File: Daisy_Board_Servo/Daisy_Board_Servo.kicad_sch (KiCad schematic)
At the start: 58 parts, among them IC1 PCA9685PW, IC2 TJA1050T_CM, IC3 LSM6DS3TR-C, J1 SM04B-SRSS-TB, J10 Conn_01x03_Pin, J11 Conn_01x03_Pin, J12 Conn_01x03_Pin, J13 Conn_01x03_Pin, J14 Conn_01x03_Pin, J15 Conn_01x03_Pin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

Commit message: Done Servo
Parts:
- added C2, C3: 100nF 50V, Capacitor_SMD:C_0402_1005Metric, symbol Device:C
- added D3: SS34, Diode_SMD:D_SOD-123, symbol Diode:1N5820
- added D4: ESD9XD, Diode_SMD:D_SOD-523, symbol Device:D
- added D5: ESD9X, Diode_SMD:D_SOD-523, symbol Device:D
- added IC4: ACS712ELCTR-05B-T, SOIC127P600X175-8N, symbol SamacSys_Parts:ACS712ELCTR-05B-T
- added JP3: SolderJumper_3_Bridged12, Jumper:SolderJumper-3_P1.3mm_Bridged2Bar12_RoundedPad1.0x1.5mm, symbol Jumper:SolderJumper_3_Bridged12
- added JP5: SolderJumper_2_Open, Jumper:SolderJumper-2_P1.3mm_Open_RoundedPad1.0x1.5mm, symbol Jumper:SolderJumper_2_Open
- added R24: 22k, Resistor_SMD:R_0402_1005Metric, symbol Device:R
- added R25: 2.2k, Resistor_SMD:R_0402_1005Metric, symbol Device:R
- added VR2: ~, Library:EY9 reg board, symbol Personal:Reg_Board
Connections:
- net +24V: now also D3.2 (A), JP3.3 (B)
- net +3.3V: now also D4.1 (K)
- net +5V: now also IC4.8 (VCC), JP5.2 (B)
- net GND: now also C2.2, C3.2, D5.2 (A), IC4.3 (IP-_1), IC4.4 (IP-_2), IC4.5 (GND), R24.2, VR2.1 (Out-), VR2.4 (In-); no longer J10.1 (Pin_1), J11.1 (Pin_1), J12.1 (Pin_1), J13.1 (Pin_1), J14.1 (Pin_1), J15.1 (Pin_1), J3.1 (Pin_1), J9.1 (Pin_1)
- net ServoPower: now also JP3.2 (C)
- net Current Sense: now reaches U1.1 (A5_GPIO5_MISO)
- net Current Sense: now also C3.1, D4.2 (A), D5.1 (K), R24.1, R25.1
- new net: C2.1, IC4.6 (FILTER)
- new net: JP3.1 (A), JP5.1 (A), VR2.2 (Out+)
- new net: IC4.7 (VIOUT), R25.2
- new net: D3.1 (K), VR2.3 (In+)
- new net ServoGND: IC4.1 (IP+_1), IC4.2 (IP+_2), J10.1 (Pin_1), J11.1 (Pin_1), J12.1 (Pin_1), J13.1 (Pin_1), J14.1 (Pin_1), J15.1 (Pin_1), J3.1 (Pin_1), J9.1 (Pin_1)
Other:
- moved on the sheet: C1, J10, J11, J12, J13, J14, J15, J3, J9, R18, R19, R20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

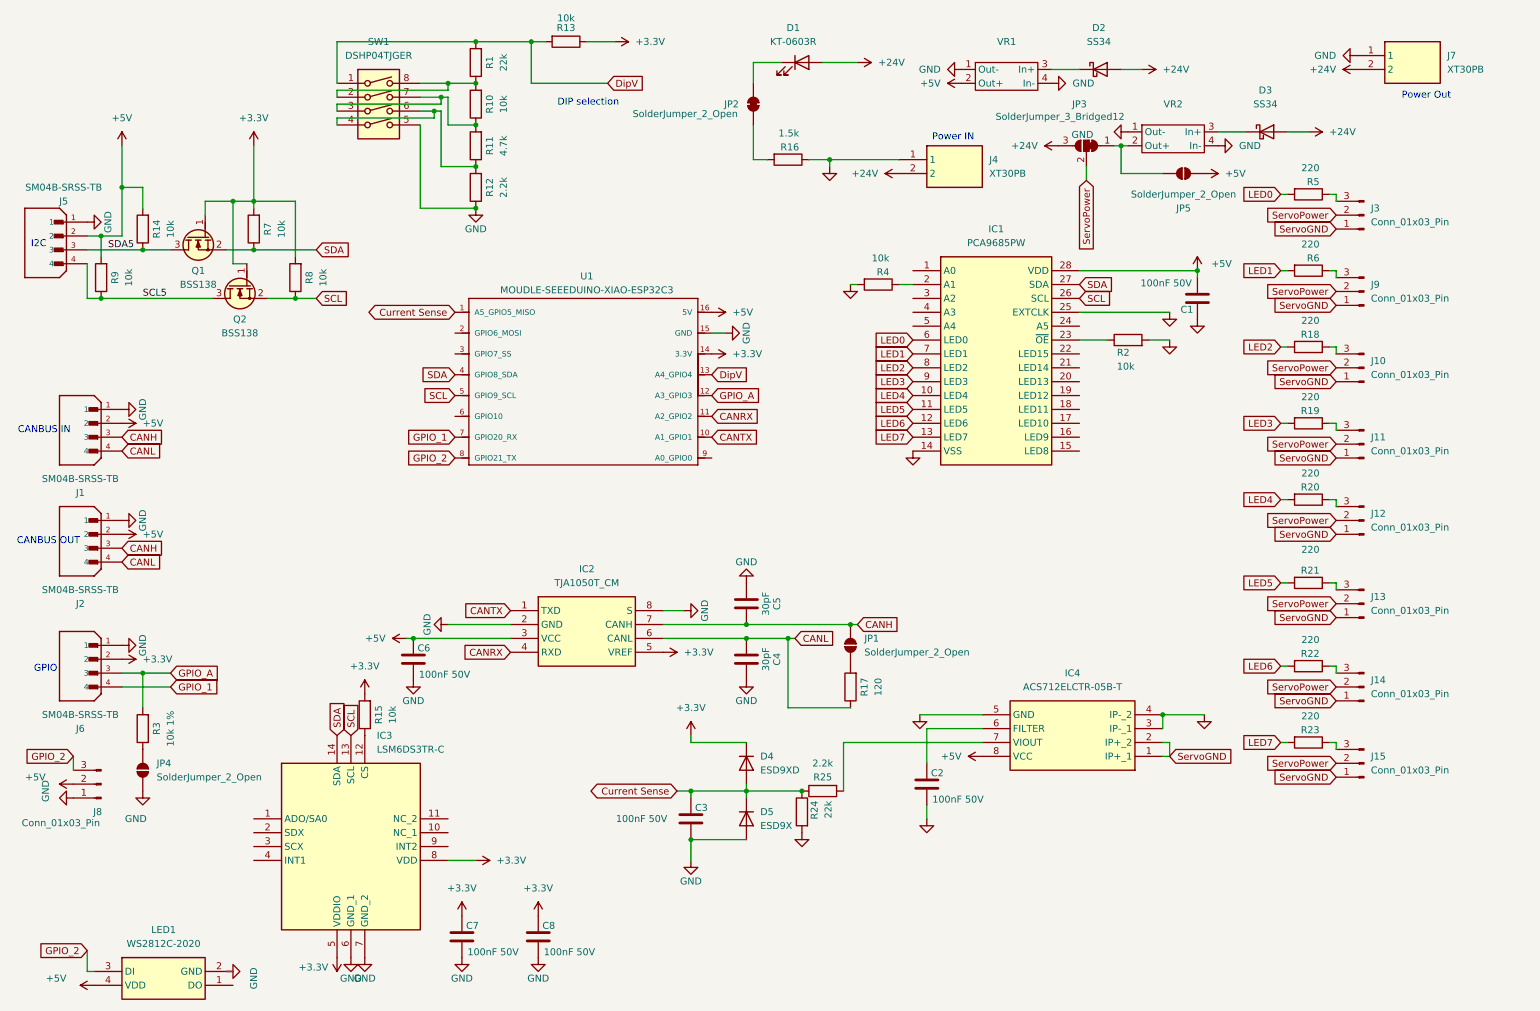
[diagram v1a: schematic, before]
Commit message: panel updates for lower QTY parts
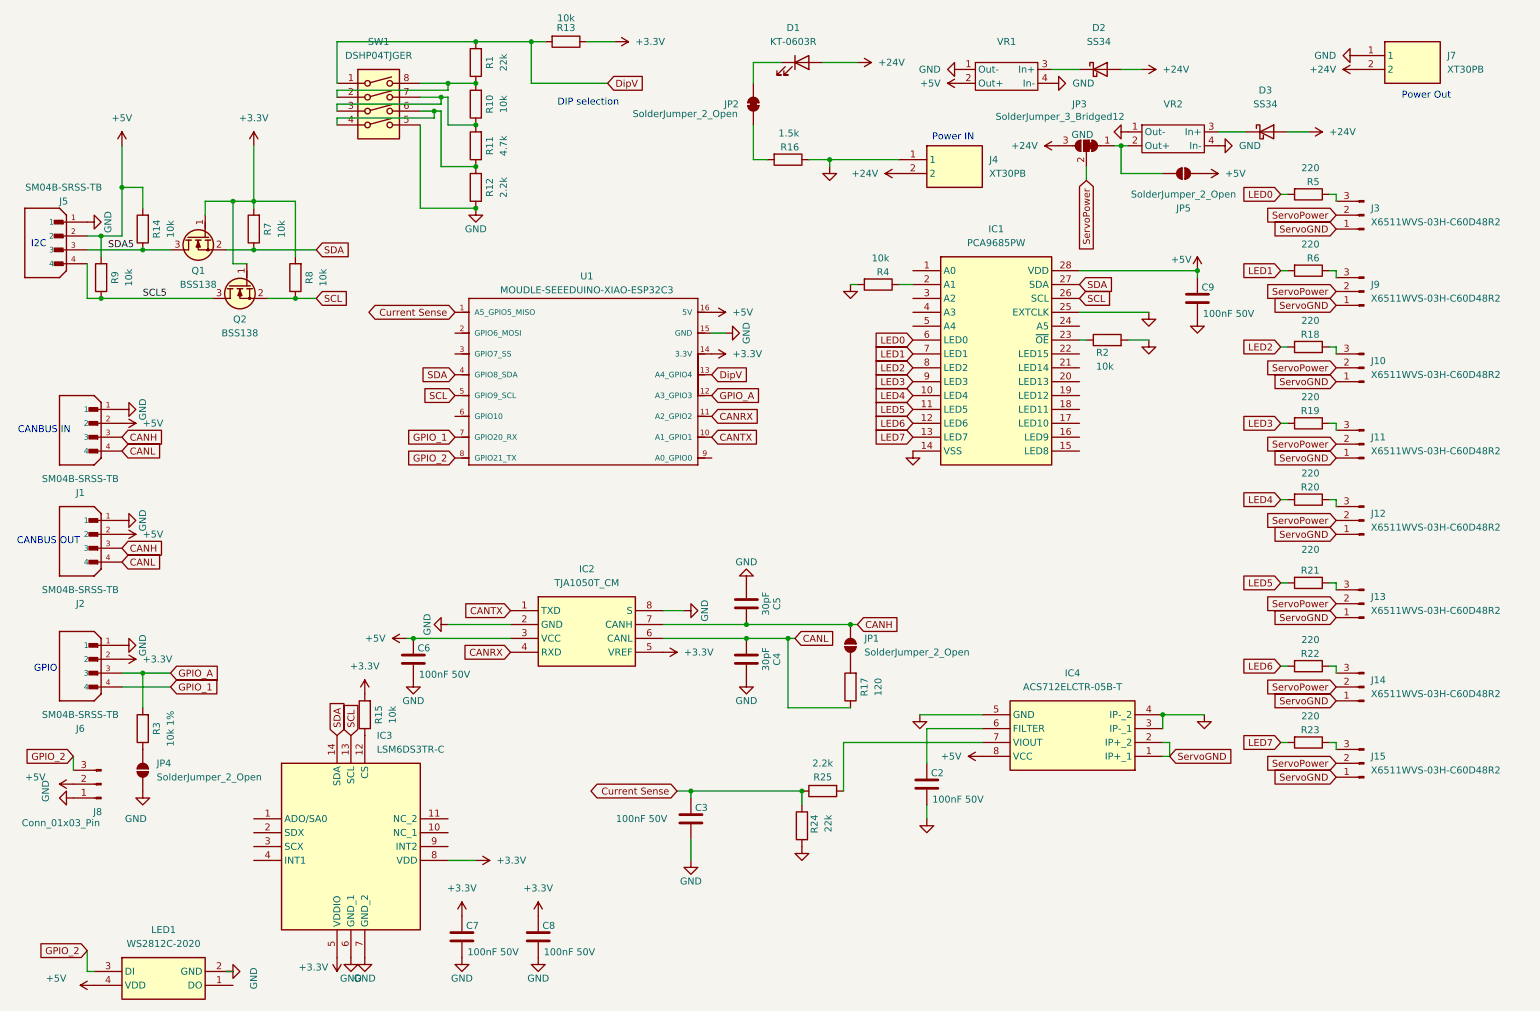
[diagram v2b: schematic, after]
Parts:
- removed C1: 100nF 50V, Capacitor_SMD:C_1206_3216Metric, symbol Device:C
- removed D4: ESD9XD, Diode_SMD:D_SOD-523, symbol Device:D
- removed D5: ESD9X, Diode_SMD:D_SOD-523, symbol Device:D
- added C9: 100nF 50V, Capacitor_SMD:C_0402_1005Metric, symbol Device:C
- J10, J11, J12, J13, J14, J15, J3, J9: value Conn_01x03_Pin -> X6511WVS-03H-C60D48R2
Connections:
- net +5V: now also C9.1
- net GND: now also C9.2
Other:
- moved on the sheet: R2, R24
